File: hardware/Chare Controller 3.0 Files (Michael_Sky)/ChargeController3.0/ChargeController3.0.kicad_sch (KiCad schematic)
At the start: 0 parts

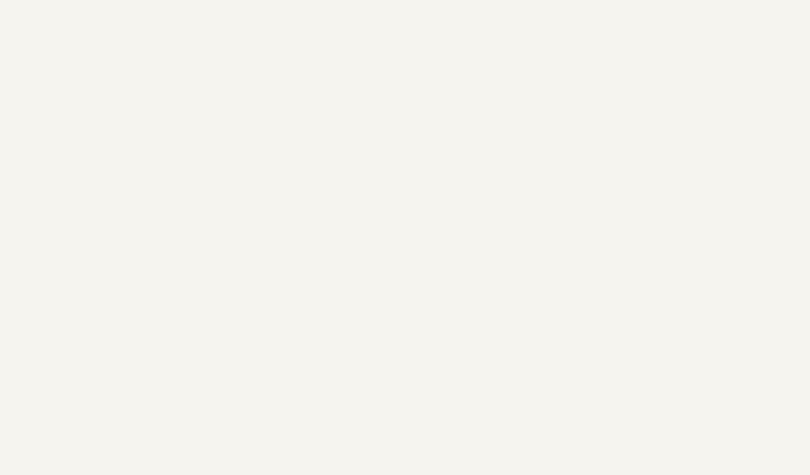
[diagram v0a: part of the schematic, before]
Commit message: moved pins to sep page
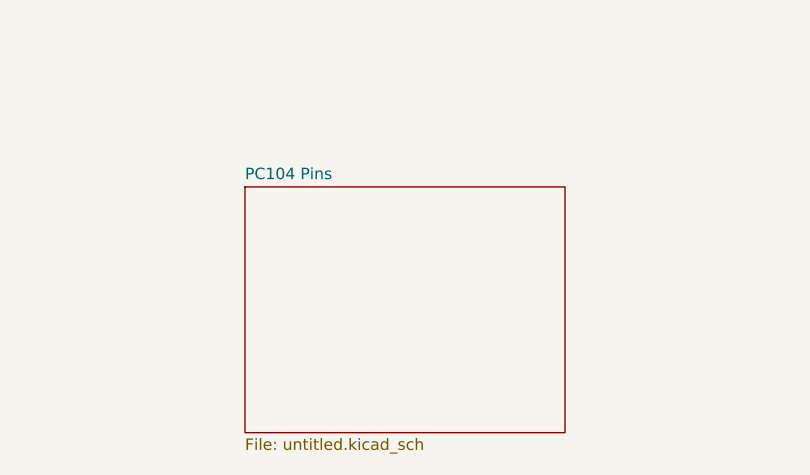
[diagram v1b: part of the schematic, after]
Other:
- added sheet PC104 Pins (untitled.kicad_sch)
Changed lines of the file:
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@@
+		)
+	)
+	(sheet
+		(at 40.005 139.7)
+		(size 35.56 27.305)
+		(exclude_from_sim no)
+		(in_bom yes)
+		(on_board yes)
+		(dnp no)
+		(fields_autoplaced yes)
+		(stroke
+			(width 0.1524)
+			(type solid)
+		)
+		(fill
+			(color 0 0 0 0.0000)
+		)
+		(property "Sheetname" "PC104 Pins"
+			(at 40.005 138.9884 0)
+			(effects
+				(font
+					(size 1.27 1.27)
+				)
+				(justify left bottom)
+			)
+		)
+		(property "Sheetfile" "untitled.kicad_sch"
+			(at 40.005 167.5896 0)
+			(effects
+				(font
+					(size 1.27 1.27)
+				)
+				(justify left top)
+			)
+		)
+		(instances
+			(project "ChargeController3.0"
+				(path "/a54826c2-d365-4450-b7a8-71945dba02c0"
+					(page "8")
+				)
+			)
 		)
 	)

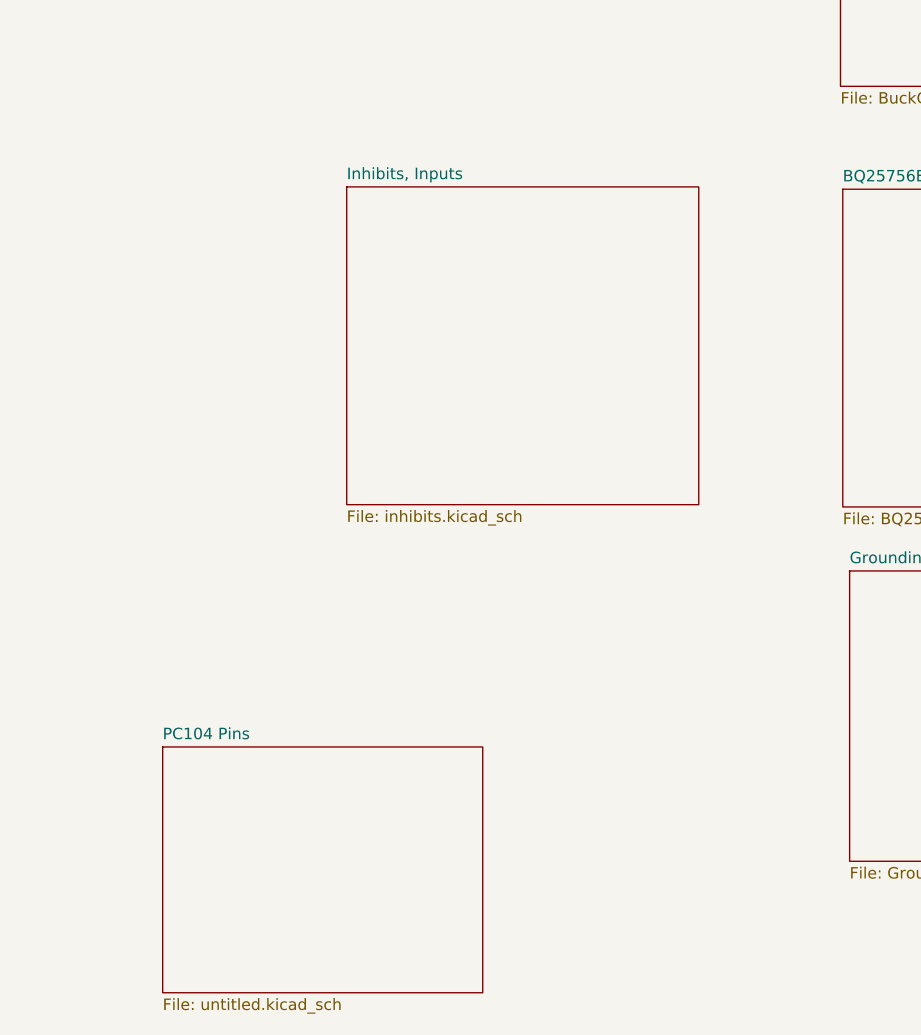
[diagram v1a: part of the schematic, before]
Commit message: Grounding and Filtering, 3.0 Inhibits Updated
Grounding and Filtering, 3.0 Inhibits Updated
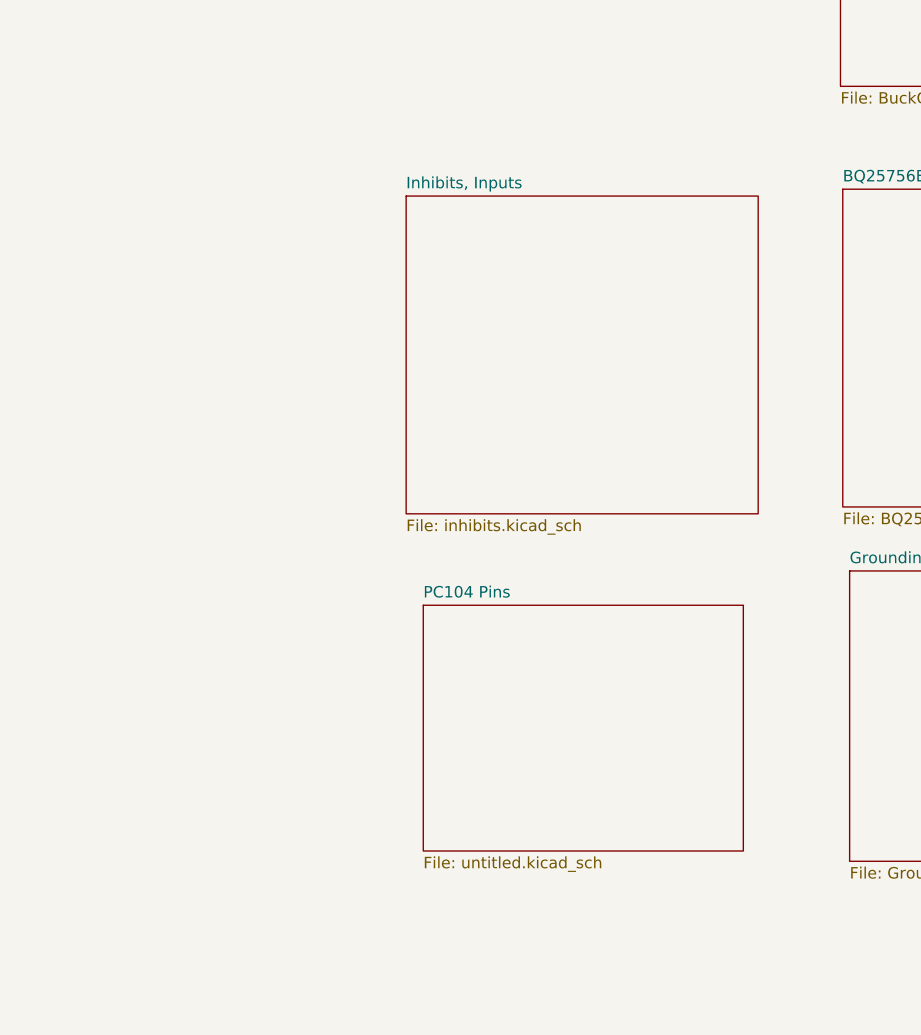
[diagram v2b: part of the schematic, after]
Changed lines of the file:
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@@
 (kicad_sch
-	(version 20250114)
+	(version 20260306)
 	(generator "eeschema")
-	(generator_version "9.0")
+	(generator_version "10.0")
 	(paper "A4")
 	(text "Battery Management System\n"
@@
 		)
 		(fill
-			(color 0 0 0 0.0000)
+			(color 0 0 0 0)
 		)
 		(property "Sheetname" "Temperature Management"
 			(at 157.48 106.4764 0)
+			(show_name no)
+			(do_not_autoplace no)
 			(effects
 				(font
@@
 		(property "Sheetfile" "TempManager.kicad_sch"
 			(at 157.48 129.3626 0)
+			(show_name no)
+			(do_not_autoplace no)
 			(effects
 				(font
@@
 	)
 	(sheet
-		(at 60.452 77.47)
+		(at 67.056 78.486)
 		(size 39.116 35.306)
 		(exclude_from_sim no)
@@
 		)
 		(fill
-			(color 0 0 0 0.0000)
+			(color 0 0 0 0)
 		)
 		(property "Sheetname" "Inhibits, Inputs"
-			(at 60.452 76.7584 0)
+			(at 67.056 77.7744 0)
+			(show_name no)
+			(do_not_autoplace no)
 			(effects
 				(font
@@
 		)
 		(property "Sheetfile" "inhibits.kicad_sch"
-			(at 60.452 113.3606 0)
+			(at 67.056 114.3766 0)
+			(show_name no)
+			(do_not_autoplace no)
 			(effects
 				(font
@@
 		)
 		(fill
-			(color 0 0 0 0.0000)
+			(color 0 0 0 0)
 		)
 		(property "Sheetname" "Buck Converter"
 			(at 115.316 34.3404 0)
+			(show_name no)
+			(do_not_autoplace no)
 			(effects
 				(font
@@
 		(property "Sheetfile" "BuckConverter.kicad_sch"
 			(at 115.316 66.8786 0)
+			(show_name no)
+			(do_not_autoplace no)
 			(effects
 				(font
@@
 		)
 		(fill
-			(color 0 0 0 0.0000)
+			(color 0 0 0 0)
 		)
 		(property "Sheetname" "Communication Interface"
 			(at 157.988 77.7744 0)
+			(show_name no)
+			(do_not_autoplace no)
 			(effects
 				(font
@@
 		(property "Sheetfile" "CommInterface.kicad_sch"
 			(at 157.988 99.6446 0)
+			(show_name no)
+			(do_not_autoplace no)
 			(effects
 				(font
@@
 		)
 		(fill
-			(color 0 0 0 0.0000)
+			(color 0 0 0 0)
 		)
 		(property "Sheetname" "BQ25756E"
 			(at 115.57 77.0124 0)
+			(show_name no)
+			(do_not_autoplace no)
 			(effects
 				(font
@@
 		(property "Sheetfile" "BQ25756E.kicad_sch"
 			(at 115.57 113.6146 0)
+			(show_name no)
+			(do_not_autoplace no)
 			(effects
 				(font
@@
 		)
 		(fill
-			(color 0 0 0 0.0000)
+			(color 0 0 0 0)
 		)
 		(property "Sheetname" "Grounding"
 			(at 116.332 119.4304 0)
+			(show_name no)
+			(do_not_autoplace no)
 			(effects
 				(font
@@
 		(property "Sheetfile" "Ground.kicad_sch"
 			(at 116.332 152.9846 0)
+			(show_name no)
+			(do_not_autoplace no)
 			(effects
 				(font
@@
 	)
 	(sheet
-		(at 40.005 139.7)
+		(at 68.961 123.952)
 		(size 35.56 27.305)
 		(exclude_from_sim no)
@@
 		)
 		(fill
-			(color 0 0 0 0.0000)
+			(color 0 0 0 0)
 		)
 		(property "Sheetname" "PC104 Pins"
-			(at 40.005 138.9884 0)
+			(at 68.961 123.2404 0)
+			(show_name no)
+			(do_not_autoplace no)
 			(effects
 				(font
@@
 		)
 		(property "Sheetfile" "untitled.kicad_sch"
-			(at 40.005 167.5896 0)
-			(effects
-				(font
+			(at 68.961 151.8416 0)
+			(show_name no)
+			(do_not_autoplace no)
+			(effects
+				(font
